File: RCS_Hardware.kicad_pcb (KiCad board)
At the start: 2 copper layers, 167.9 x 119.9 mm, 39 parts, among them J1 SWD, J2 TYPE-C-31-M-12, U1 STM32F401CCU6, U2 AMS1117-3.3, U3 BMP280, U4 BNO055, Y1 16MHz, Y2 32.768Mhz

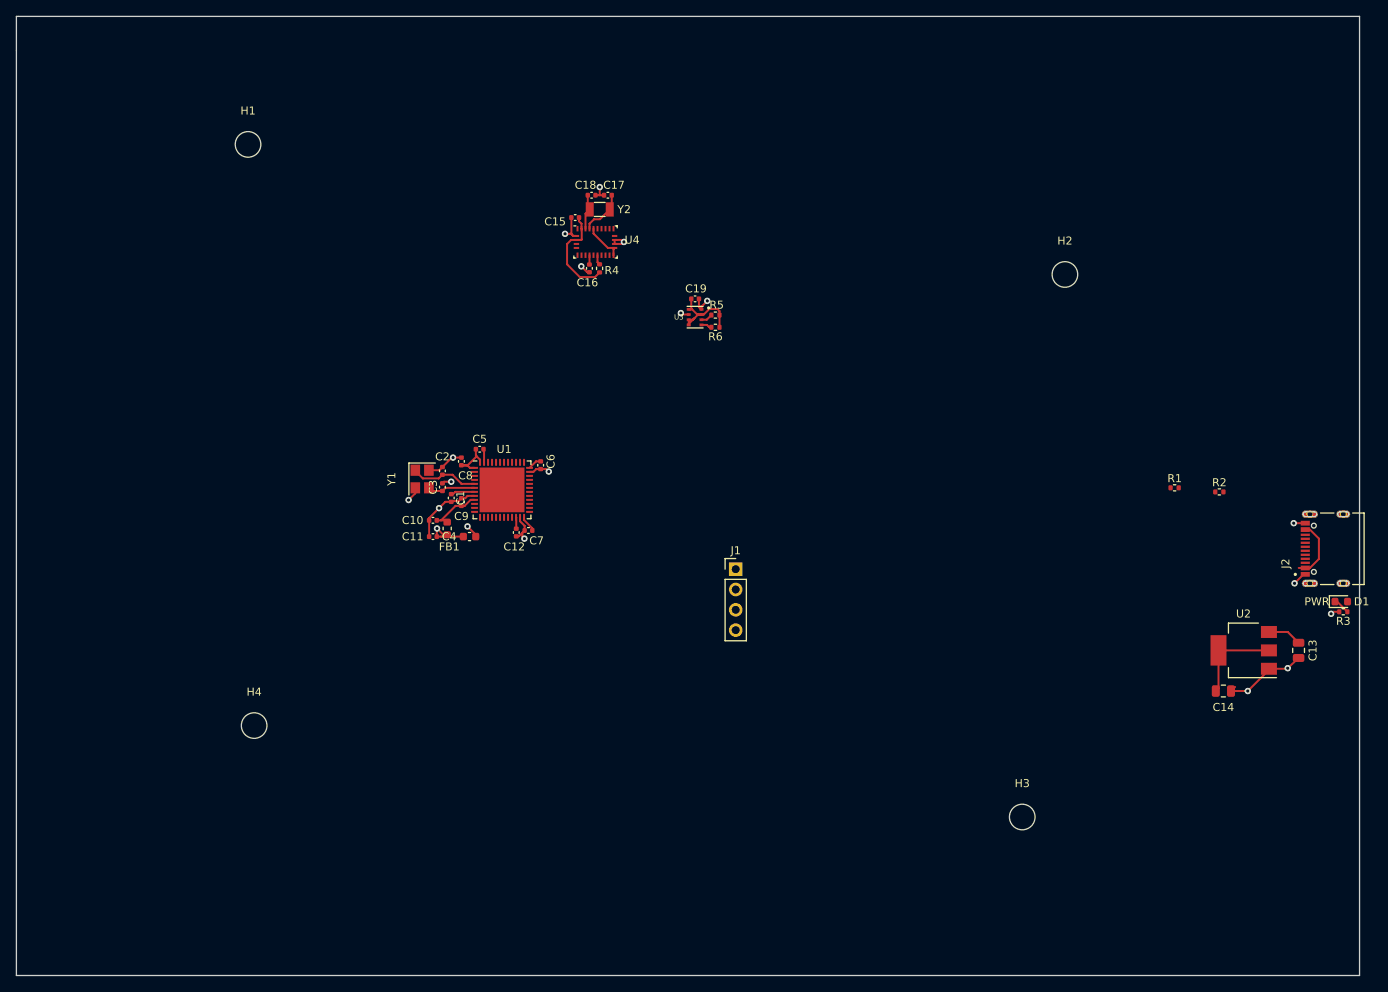
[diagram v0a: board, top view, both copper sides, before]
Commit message: added SPI NOR flash chip fixed minor issues with BNO055 schema completed a rough layout of the entire current pcb
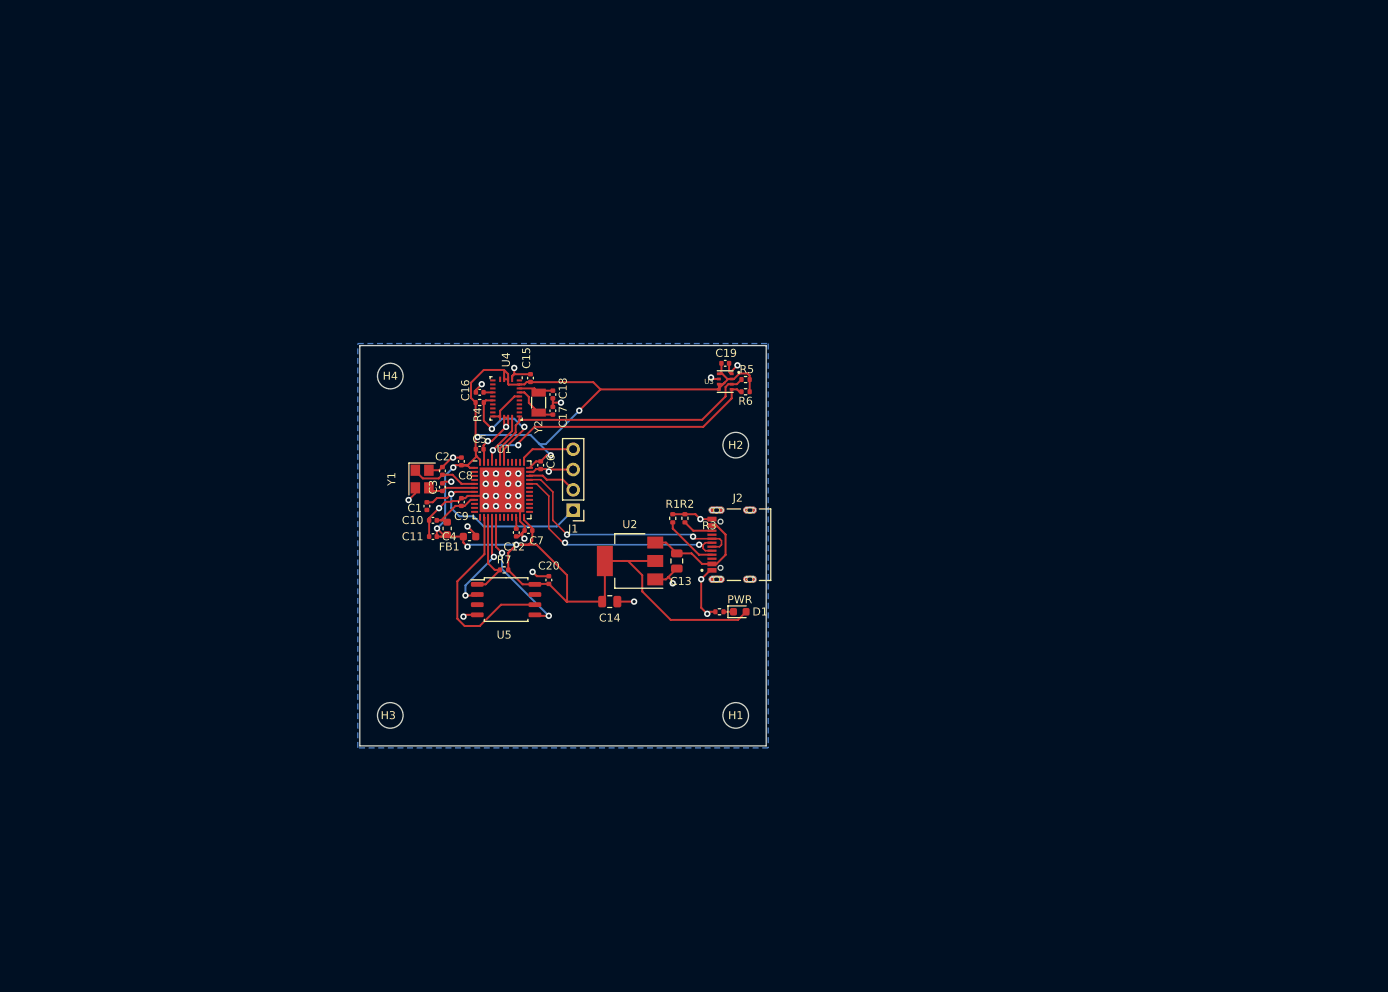
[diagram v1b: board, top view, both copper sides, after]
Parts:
- added C20: 100nF, Capacitor_SMD:C_0402_1005Metric, F.Cu at (134.9, 103.7)
- added R7: 10k, Resistor_SMD:R_0402_1005Metric, F.Cu at (129.3, 102.5)
- added U5: W25Q32JVSS, Package_SO:SOIC-8_5.23x5.23mm_P1.27mm, F.Cu at (129.5, 106.2)
- moved H1 93.9 mm to (158.2, 120.7)
- moved H3 80.0 mm to (115.1, 120.7)
- moved C13 78.5 mm to (150.9, 101.3)
- moved R3 78.0 mm to (156.2, 107.7)
- moved C14 77.5 mm to (142.5, 106.4)
- moved U2 77.5 mm to (145.0, 101.3)
- moved D1 75.2 mm to (158.8, 107.7)
- moved J2 74.2 mm to (160.0, 99.3)
- moved R2 66.9 mm to (151.9, 96.0), turned to -90 degrees
- moved R1 62.9 mm to (150.4, 96.0), turned to -90 degrees
- moved H4 46.9 mm to (115.1, 78.2)
- moved H2 46.4 mm to (158.2, 86.9)
- moved C17 27.8 mm to (135.4, 82.6), turned to 90 degrees
- moved C18 25.4 mm to (135.4, 80.5), turned to -90 degrees
- moved Y2 25.3 mm to (133.6, 81.6), turned to 90 degrees
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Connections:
- C15 pad 1: Net-(C15-Pad1) -> +3.3V
- R4 pad 1: Net-(C15-Pad1) -> +3.3V
- U1 pad 14: unconnected-(U1-Pad14) -> /CS_FLASH
- U1 pad 15: unconnected-(U1-Pad15) -> /SCLK
- U1 pad 16: unconnected-(U1-Pad16) -> /MISO
- U1 pad 17: unconnected-(U1-Pad17) -> /MOSI
- U4 pad 28: Net-(C15-Pad1) -> +3.3V
- U4 pad 3: Net-(C15-Pad1) -> +3.3V
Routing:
- net +3.3V: track 39.2 -> 174.8 mm, vias 1 -> 7
- net /SCL: track 1.35 -> 41.8 mm, vias 0 -> 2
- net /SDA: track 1.47 -> 37.3 mm
- net /USB_D+: track 0.00 -> 31.0 mm, vias 0 -> 2
- net /USB_D-: track 0.00 -> 30.2 mm, vias 0 -> 2
- net /CS_FLASH: track 0.00 -> 25.3 mm
- net GND: track 57.9 -> 81.4 mm, vias 18 -> 37
- net /NRST: track 3.03 -> 25.3 mm, vias 0 -> 1
- net /MOSI: track 0.00 -> 16.8 mm, vias 0 -> 2
- net /BNO_NRST: track 1.24 -> 15.5 mm, vias 0 -> 2
- net /MISO: track 0.00 -> 12.9 mm, vias 0 -> 2
- net Net-(C15-Pad1): track 12.4 -> 0.00 mm
- net /SCLK: track 0.00 -> 11.2 mm
- net /SWCLK: track 0.00 -> 7.16 mm
- net Net-(R1-Pad2): track 0.00 -> 7.02 mm
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- added copper zone on B.Cu, net GND
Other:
- board size 167.9 x 119.9 mm -> 50.8 x 50 mm
- board text added: "ACC2"
- board text added: "SOLENOID CONTROL"

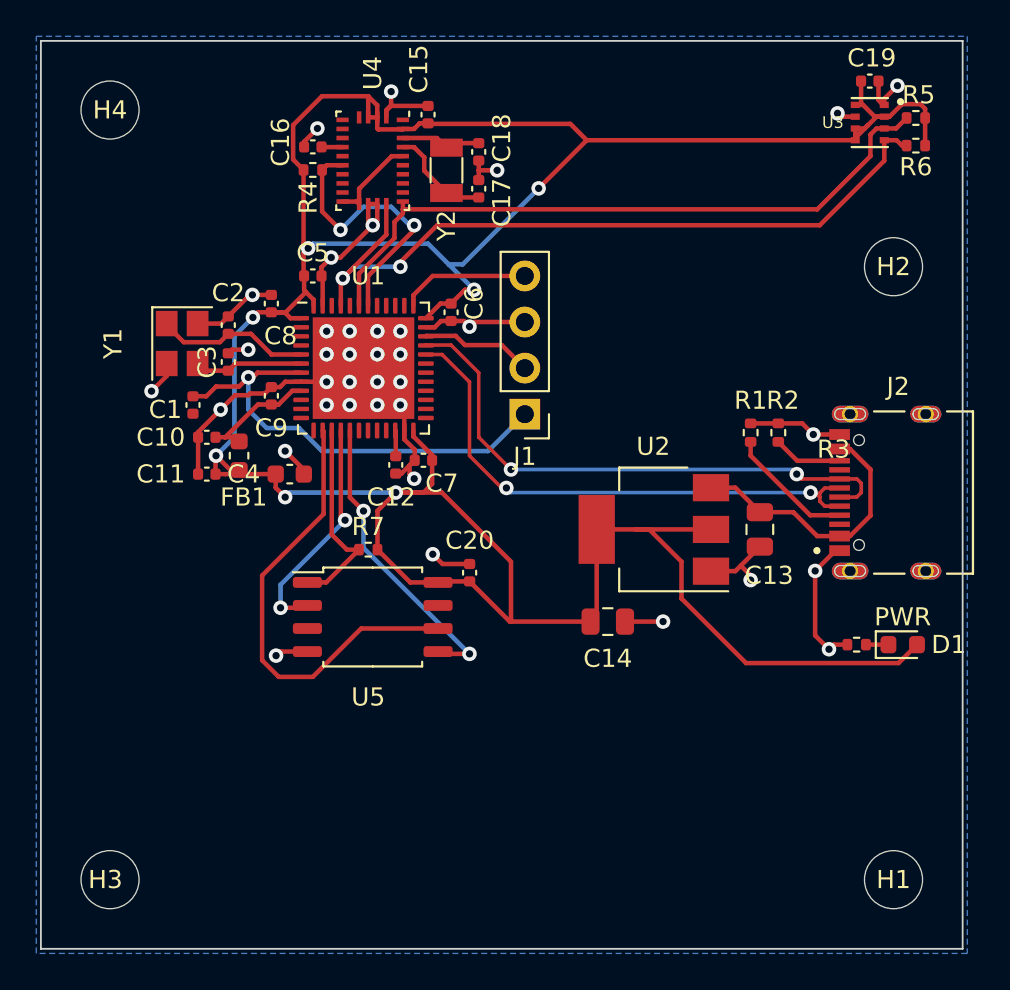
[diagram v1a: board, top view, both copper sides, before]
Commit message: Added External Power Support Added layout for external Power Updated SilkScreen Fixed Mounting hole layout Added render of board
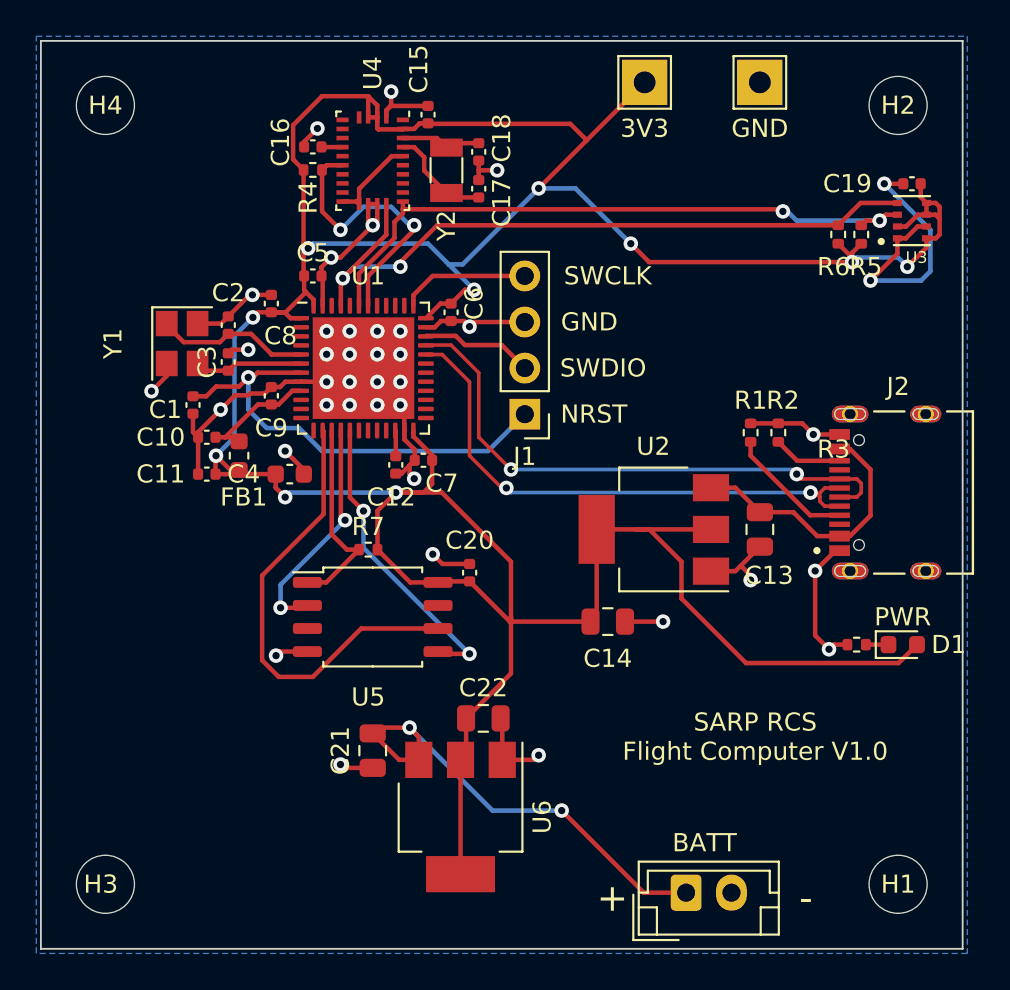
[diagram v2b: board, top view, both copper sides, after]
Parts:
- added 3V3: 3V3, TestPoint:TestPoint_THTPad_2.5x2.5mm_Drill1.2mm, F.Cu at (144.5, 76.7)
- added BATT: JST BATT, Connector_JST:JST_EH_B2B-EH-A_1x02_P2.50mm_Vertical, F.Cu at (146.8, 121.4)
- added C21: 22uF, Capacitor_SMD:C_0805_2012Metric, F.Cu at (129.5, 113.5)
- added C22: 22uF, Capacitor_SMD:C_0805_2012Metric, F.Cu at (135.6, 111.8)
- added GND: GND, TestPoint:TestPoint_THTPad_2.5x2.5mm_Drill1.2mm, F.Cu at (150.9, 76.7)
- added U6: AMS1117-3.3, Package_TO_SOT_SMD:SOT-223-3_TabPin2, F.Cu at (134.4, 117.2)
- moved H2 8.89 mm to (158.5, 78.0)
- moved R5 7.09 mm to (156.5, 85.1), turned to 90 degrees
- moved R6 6.50 mm to (155.2, 85.1), turned to 90 degrees
- moved C19 6.12 mm to (159.3, 82.3), turned to 0 degrees
- moved U3 5.88 mm to (159.3, 84.3), turned to 180 degrees
- moved H1 0.36 mm to (158.5, 120.9)
- moved H4 0.36 mm to (114.8, 78.0)
- moved H3 0.36 mm to (114.8, 120.9)
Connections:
- J2 pad S1: unconnected-(J2-PadS1) -> GND
- J2 pad S2: unconnected-(J2-PadS2) -> GND
- J2 pad S3: unconnected-(J2-PadS3) -> GND
- J2 pad S4: unconnected-(J2-PadS4) -> GND
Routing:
- net +3.3V: track 174.8 -> 202.6 mm, vias 7 -> 10
- net /BATT_IN: track 0.00 -> 26.3 mm, vias 0 -> 2
- net GND: track 81.4 -> 100.2 mm, vias 37 -> 39
- net /SCL: track 41.8 -> 39.1 mm
- net /SDA: track 37.3 -> 35.5 mm, vias 0 -> 2
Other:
- board text added: "+"
- board text added: "-"
- board text added: "GND"
- board text added: "NRST"
- board text added: "SARP RCS Flight Computer V1.0"
- board text added: "SWCLK"
- board text added: "SWDIO"
- board text removed: "SOLENOID CONTROL"

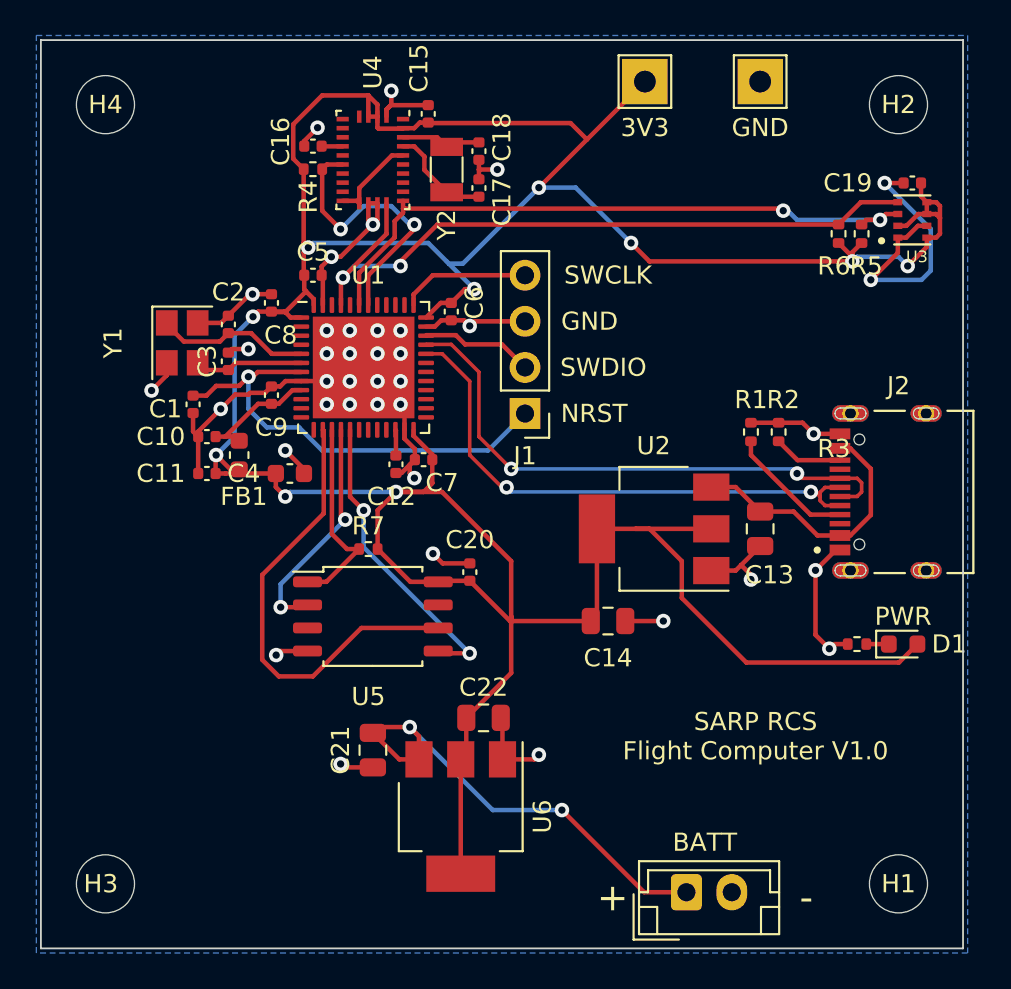
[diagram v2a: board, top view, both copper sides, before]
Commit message: added solenoid control pins added external sensor pins added green and blue status leds updated render
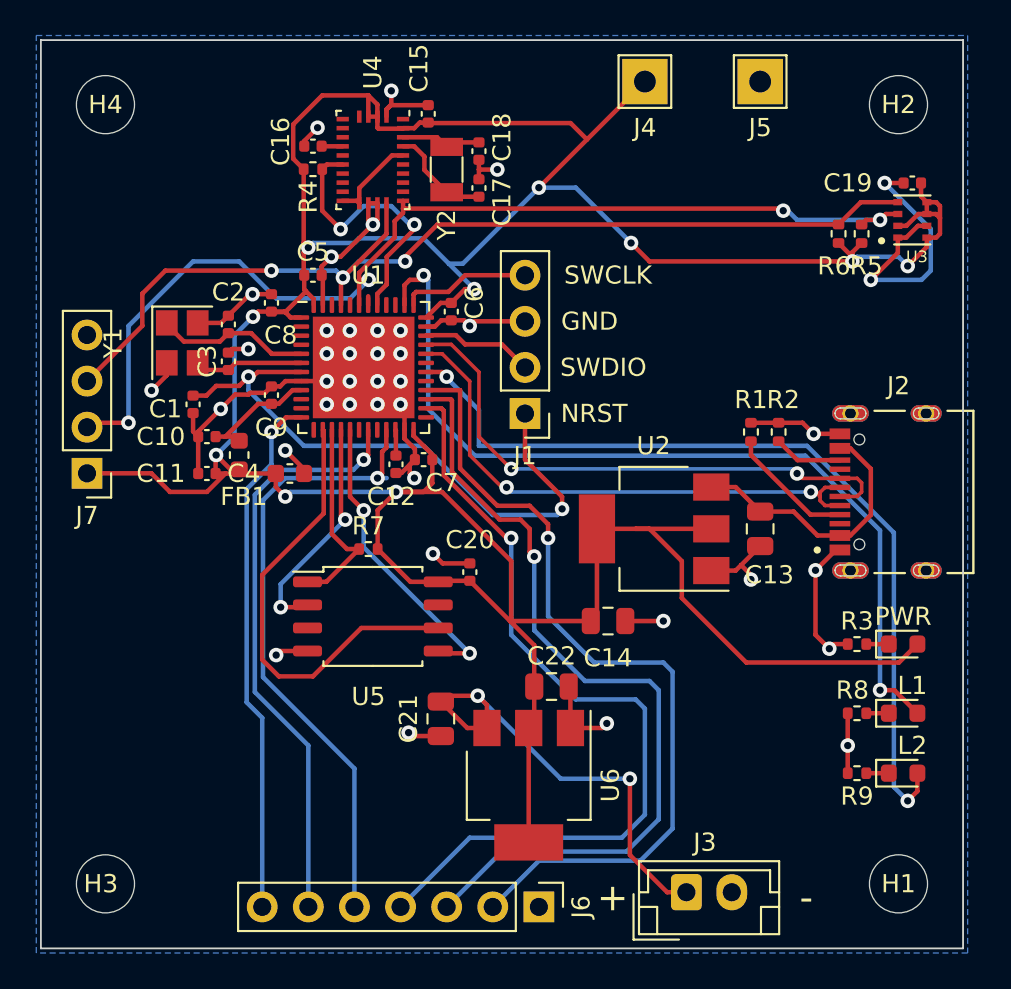
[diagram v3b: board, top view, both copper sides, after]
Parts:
- added D2: LED, LED_SMD:LED_0603_1608Metric, F.Cu at (158.8, 111.5)
- added D3: LED, LED_SMD:LED_0603_1608Metric, F.Cu at (158.8, 114.8)
- added J6: Solenoids, Connector_PinHeader_2.54mm:PinHeader_1x07_P2.54mm_Vertical, F.Cu at (138.7, 122.2)
- added J7: Ext Sesnor, Connector_PinHeader_2.54mm:PinHeader_1x04_P2.54mm_Vertical, F.Cu at (113.8, 98.3)
- added R8: 1k, Resistor_SMD:R_0402_1005Metric, F.Cu at (156.2, 111.5)
- added R9: 1k, Resistor_SMD:R_0402_1005Metric, F.Cu at (156.2, 114.8)
- moved C21 4.12 mm to (133.3, 111.8)
- moved C22 4.12 mm to (139.4, 110.0)
- moved U6 4.12 mm to (138.1, 115.5)
- renumbered BATT to J3, 3V3 to J4, GND to J5
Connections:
- U1 pad 12: unconnected-(U1-Pad12) -> /S1
- U1 pad 19: unconnected-(U1-Pad19) -> /S2
- U1 pad 21: unconnected-(U1-Pad21) -> /S3
- U1 pad 26: unconnected-(U1-Pad26) -> /S4
- U1 pad 27: unconnected-(U1-Pad27) -> /S5
- U1 pad 28: unconnected-(U1-Pad28) -> /S6
- U1 pad 30: unconnected-(U1-Pad30) -> /LED_B
- U1 pad 38: unconnected-(U1-Pad38) -> /LED_G
- U1 pad 41: unconnected-(U1-Pad41) -> /BNO_NRST
- U1 pad 42: /BNO_NRST -> unconnected-(U1-Pad42)
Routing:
- net /LED_G: track 0.00 -> 49.0 mm, vias 0 -> 2
- net /LED_B: track 0.00 -> 47.5 mm, vias 0 -> 2
- net /S6: track 0.00 -> 45.8 mm, vias 0 -> 1
- net /S4: track 0.00 -> 45.8 mm, vias 0 -> 1
- net /S5: track 0.00 -> 45.7 mm, vias 0 -> 1
- net /S3: track 0.00 -> 34.7 mm, vias 0 -> 1
- net /S2: track 0.00 -> 32.5 mm, vias 0 -> 1
- net /S1: track 0.00 -> 29.1 mm, vias 0 -> 1
- net /SDA: track 35.5 -> 59.8 mm, vias 2 -> 4
- net /SCL: track 39.1 -> 56.9 mm, vias 2 -> 3
- net /NRST: track 25.3 -> 33.8 mm, vias 1 -> 2
- net +3.3V: track 202.6 -> 208.9 mm
- net GND: track 100.2 -> 103.5 mm, vias 39 -> 40
- net Net-(D3-Pad1): track 0.00 -> 1.24 mm
- net Net-(D2-Pad1): track 0.00 -> 1.24 mm
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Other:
- board text added: "L1"
- board text added: "L2"
